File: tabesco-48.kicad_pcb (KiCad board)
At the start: 2 copper layers, 192.5 x 118.4 mm, 98 parts, among them SW1 SW_Push, U1 ProMicro

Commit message: created tabesco-31
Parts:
- removed D32, D33, D34, D35, D36, D37, D38, D39, D40, D41, D42, D43, D44, D45, D46, D47, D48: D_Small, Diode_SMD:D_SOD-123
- removed MX32, MX33, MX34, MX35, MX36, MX37, MX38, MX39, MX40, MX41, MX42, MX43, MX44, MX45, MX46, MX47, MX48: MX_SW_HS, marbastlib-mx:SW_MX_HS_CPG151101S11_1u
- added REF**: STAB_MX_6u, marbastlib-mx:STAB_MX_6u, F.Cu at (146.0, 89.3)
- U1: moved to B.Cu
- moved D1 182.9 mm to (60.3, 38.2), turned to 90 degrees
- moved MX1 182.5 mm to (60.3, 32.2)
- moved D11 178.2 mm to (65.0, 57.2), turned to 90 degrees
- moved MX11 177.8 mm to (65.0, 51.2)
- moved D10 164.7 mm to (231.7, 38.2), turned to 90 degrees
- moved MX10 164.3 mm to (231.7, 32.2)
- moved D30 164.1 mm to (79.3, 95.3), turned to 90 degrees
- moved MX30 163.6 mm to (79.3, 89.3)
- moved MX21 154.2 mm to (79.3, 70.3)
- moved D2 145.4 mm to (79.3, 38.2), turned to 90 degrees
- moved MX2 144.8 mm to (79.3, 32.2)
- moved D19 141.3 mm to (227.0, 57.2), turned to 90 degrees
- moved MX19 140.8 mm to (227.0, 51.2)
- moved D12 136.0 mm to (88.8, 57.2), turned to 90 degrees
- moved MX12 135.5 mm to (88.8, 51.2)
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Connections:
- D20 pad 1: /row1 -> /row2
- D29 pad 1: /row2 -> /row3
- MX20 pad 2: /col9 -> /col0
- MX21 pad 2: /col0 -> /col1
- MX22 pad 2: /col1 -> /col2
- MX23 pad 2: /col2 -> /col3
- MX24 pad 2: /col3 -> /col4
- MX25 pad 2: /col4 -> /col5
- MX26 pad 2: /col5 -> /col6
- MX27 pad 2: /col6 -> /col7
- MX28 pad 2: /col7 -> /col8
- MX29 pad 2: /col8 -> /col0
- MX30 pad 2: /col0 -> /col1
- MX31 pad 2: /col1 -> /col7
- U1 pad 5: /col_tmo -> unconnected-(U1-D1-Pad5)
- U1 pad 6: /row4 -> unconnected-(U1-D0-Pad6)
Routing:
- net /row4: track 292.9 -> 0.00 mm
- net /row3: track 276.5 -> 19.0 mm
- net /col8: track 228.5 -> 0.00 mm
- net /col7: track 211.5 -> 0.00 mm
- net /col9: track 209.3 -> 0.00 mm
- net /col6: track 195.2 -> 0.00 mm
- net /col5: track 176.7 -> 0.00 mm
- net /col4: track 157.6 -> 0.00 mm
- net /col3: track 142.6 -> 0.00 mm
- net /col2: track 136.9 -> 0.00 mm
- net /col0: track 111.3 -> 0.00 mm
- net /col1: track 96.1 -> 0.00 mm
- net /row2: track 243.4 -> 161.9 mm
- net /row1: track 242.0 -> 161.9 mm
- net GND: track 54.7 -> 0.00 mm
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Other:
- board size 192.5 x 118.4 mm -> 190.5 x 86.7 mm
- board text removed: "tabesco-48"

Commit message: work on 31
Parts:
- moved D28 123.8 mm to (222.2, 76.3)
- moved D27 114.3 mm to (193.6, 76.3)
- moved D26 47.6 mm to (174.6, 76.3)
- moved D23 38.1 mm to (117.4, 76.3)
- moved D21 38.1 mm to (79.3, 76.3)
- moved D22 38.1 mm to (98.4, 76.3)
- moved D24 38.1 mm to (136.5, 76.3)
- moved D25 38.1 mm to (155.5, 76.3)
- moved SW1 3.93 mm to (230.8, 95.7)
- moved U1 3.93 mm to (224.4, 93.2)
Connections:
- MX31 pad 2: /col7 -> /col5
- U1 pad 10: /row0 -> /col5
- U1 pad 11: /col0 -> /col6
- U1 pad 12: /col1 -> /col7
- U1 pad 17: /col2 -> /row0
- U1 pad 18: /col3 -> /row1
- U1 pad 19: /col4 -> /row2
- U1 pad 20: /col5 -> /row3
- U1 pad 21: /col6 -> unconnected-(U1-B1-Pad21)
- U1 pad 22: /col7 -> unconnected-(U1-B3-Pad22)
- U1 pad 5: unconnected-(U1-D1-Pad5) -> /col0
- U1 pad 6: unconnected-(U1-D0-Pad6) -> /col1
- U1 pad 7: /row3 -> /col2
- U1 pad 8: /row2 -> /col3
- U1 pad 9: /row1 -> /col4
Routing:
- net /col0: track 0.00 -> 308.7 mm
- net /col1: track 0.00 -> 296.8 mm
- net /col2: track 0.00 -> 260.0 mm
- net /row0: track 171.4 -> 416.5 mm
- net /col3: track 0.00 -> 242.2 mm
- net /col5: track 0.00 -> 231.9 mm
- net /row1: track 161.9 -> 388.4 mm
- net /col4: track 0.00 -> 224.5 mm
- net /row2: track 161.9 -> 361.3 mm
- net /col6: track 0.00 -> 188.7 mm
- net /col7: track 0.00 -> 171.2 mm
- net /col8: track 0.00 -> 167.7 mm
- net /row3: track 19.0 -> 166.4 mm
- net /col9: track 0.00 -> 96.6 mm
- net GND: track 0.00 -> 27.5 mm
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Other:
- board size 190.5 x 86.7 mm -> 196.2 x 86.7 mm

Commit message: tabesco31 pcb done(?)
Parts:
- removed SW1: SW_Push, Button_Switch_THT:SW_Tactile_Straight_KSA0Axx1LFTR
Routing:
- net RST: track 13.8 -> 0.00 mm
- net GND: track 27.5 -> 18.8 mm
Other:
- board text added: "swag bord"
- board text added: "tabesco-31"

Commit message: more work, transitioning to IC in seperate repo
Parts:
- added D32: D_Small, Diode_SMD:D_SOD-123, B.Cu at (166.9, 135.7)
- added D34: D_Small, Diode_SMD:D_SOD-123, B.Cu at (233.6, 135.7)
- added MX32: MX_SW_HS, marbastlib-mx:SW_MX_HS_CPG151101S11_1u, B.Cu at (166.9, 129.7)
- added MX32-2: MX_SW_HS, marbastlib-mx:SW_MX_HS_CPG151101S11_1u, B.Cu at (176.4, 129.7)
- added MX34: MX_SW_HS, marbastlib-mx:SW_MX_HS_CPG151101S11_1u, B.Cu at (233.6, 129.7)
- moved U1 109.3 mm to (123.9, 136.1)
- moved D31 61.1 mm to (100.2, 135.7)
- moved MX31 61.1 mm to (100.2, 129.7)
- moved REF** 45.5 mm to (166.9, 129.7)
- moved D1 40.4 mm to (62.1, 78.6)
- moved D10 40.4 mm to (233.6, 78.6)
- moved D2 40.4 mm to (81.2, 78.6)
- moved D3 40.4 mm to (100.2, 78.6)
- moved D4 40.4 mm to (119.3, 78.6)
- moved D5 40.4 mm to (138.3, 78.6)
- moved D6 40.4 mm to (157.4, 78.6)
- moved D7 40.4 mm to (176.4, 78.6)
- moved D8 40.4 mm to (195.5, 78.6)
- moved D9 40.4 mm to (214.5, 78.6)
- moved D11 40.4 mm to (66.9, 97.6)
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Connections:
- MX31 pad 2: /col5 -> /col2
- U1 pad 11: /col6 -> /col4
- U1 pad 12: /col7 -> /col3
- U1 pad 17: /row0 -> /row3
- U1 pad 18: /row1 -> /row2
- U1 pad 19: /row2 -> /row1
- U1 pad 20: /row3 -> /row0
- U1 pad 22: unconnected-(U1-B3-Pad22) -> /col2
- U1 pad 23: /col8 -> /col1
- U1 pad 24: /col9 -> /col0
- U1 pad 5: /col0 -> unconnected-(U1-D1-Pad5)
- U1 pad 6: /col1 -> /col9
- U1 pad 7: /col2 -> /col8
- U1 pad 8: /col3 -> /col7
- U1 pad 9: /col4 -> /col6
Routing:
- net /col0: track 308.7 -> 114.7 mm
- net /col1: track 296.8 -> 104.8 mm
- net /col2: track 260.0 -> 92.9 mm
- net /col3: track 242.2 -> 77.8 mm
- net /col4: track 224.5 -> 90.2 mm
- net /row0: track 416.5 -> 302.5 mm
- net /row1: track 388.4 -> 281.7 mm
- net /row2: track 361.3 -> 259.9 mm
- net /col9: track 96.6 -> 193.1 mm
- net /col5: track 231.9 -> 141.4 mm
- net /col8: track 167.7 -> 204.4 mm
- net Net-(D32-A): track 0.00 -> 25.5 mm
- net /col6: track 188.7 -> 164.9 mm
- net /row3: track 165.9 -> 180.0 mm
- net /col7: track 171.2 -> 161.2 mm
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
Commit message: brain mode
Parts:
- U1: moved to F.Cu
- moved U1 19.3 mm to (142.4, 130.6)
- moved MX7 0.45 mm to (176.7, 72.9)
- moved MX14 0.45 mm to (129.1, 91.9)
- moved MX26 0.45 mm to (176.7, 111.0)
- moved MX28 0.45 mm to (224.4, 111.0)
- moved MX32-2 0.45 mm to (176.7, 130.0)
- moved MX4 0.45 mm to (119.6, 72.9)
- moved MX1 0.45 mm to (62.4, 72.9)
- moved MX10 0.45 mm to (233.9, 72.9)
- moved MX11 0.45 mm to (67.2, 91.9)
- moved MX12 0.45 mm to (91.0, 91.9)
- moved MX2 0.45 mm to (81.5, 72.9)
- moved MX23 0.45 mm to (119.6, 111.0)
- moved MX3 0.45 mm to (100.5, 72.9)
- moved MX5 0.45 mm to (138.6, 72.9)
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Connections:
- U1 pad 10: /col5 -> /col8
- U1 pad 11: /col4 -> /col7
- U1 pad 12: /col3 -> /col6
- U1 pad 17: /row3 -> /col2
- U1 pad 18: /row2 -> /col1
- U1 pad 19: /row1 -> /col0
- U1 pad 20: /row0 -> unconnected-(U1-F7-Pad20)
- U1 pad 21: unconnected-(U1-B1-Pad21) -> /row0
- U1 pad 22: /col2 -> /row1
- U1 pad 23: /col1 -> /row2
- U1 pad 24: /col0 -> /row3
- U1 pad 6: /col9 -> /col3
- U1 pad 7: /col8 -> /col4
- U1 pad 8: /col7 -> /col5
- U1 pad 9: /col6 -> /col9
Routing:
- net /col6: track 164.9 -> 91.9 mm
- net /col7: track 161.2 -> 107.6 mm
- net /col0: track 114.7 -> 149.0 mm
- net /col8: track 204.4 -> 170.6 mm
- net /col5: track 141.4 -> 110.8 mm
- net /row2: track 259.9 -> 288.5 mm
- net /row1: track 281.7 -> 310.3 mm
- net /row0: track 302.5 -> 330.5 mm
- net /col1: track 104.8 -> 131.2 mm
- net /col4: track 90.2 -> 64.5 mm
- net /col2: track 92.9 -> 113.6 mm
- net /col9: track 193.1 -> 174.1 mm
- net /row3: track 180.0 -> 181.6 mm
- net /col3: track 77.8 -> 76.7 mm

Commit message: finished tabesco-34
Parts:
- removed MX32-2: MX_SW_HS, marbastlib-mx:SW_MX_HS_CPG151101S11_1u
- added D33: D_Small, Diode_SMD:D_SOD-123, B.Cu at (104.1, 106.0)
- added MX11-2: MX_SW_HS, marbastlib-mx:SW_MX_HS_CPG151101S11_1u, B.Cu at (63.8, 65.9)
- added MX19-2: MX_SW_HS, marbastlib-mx:SW_MX_HS_CPG151101S11_1u, B.Cu at (221.0, 65.9)
- added MX33: MX_SW_HS, marbastlib-mx:SW_MX_HS_CPG151101S11_1u, B.Cu at (111.4, 104.0)
- added MX34-2: MX_SW_HS, marbastlib-mx:SW_MX_HS_CPG151101S11_1u, B.Cu at (178.1, 104.0)
- U1: moved to B.Cu
- moved MX29 169.4 mm to (225.7, 84.9)
- moved D29 163.7 mm to (218.4, 86.9)
- moved D32 87.1 mm to (85.0, 106.0)
- moved MX32 79.2 mm to (92.4, 104.0)
- moved D34 78.2 mm to (161.2, 106.0)
- moved MX34 70.3 mm to (168.6, 104.0)
- moved U1 69.6 mm to (206.7, 104.0)
- moved D30 45.3 mm to (46.9, 106.0)
- moved D31 45.3 mm to (66.0, 106.0)
- moved D28 38.7 mm to (199.3, 86.9)
- moved MX30 37.7 mm to (54.3, 104.0)
- moved MX31 37.7 mm to (73.3, 104.0)
- moved D19 35.8 mm to (208.9, 67.9)
- moved D1 33.4 mm to (46.9, 48.8)
- moved D10 33.4 mm to (218.4, 48.8)
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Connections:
- D29 pad 1: /row3 -> /row2
- MX29 pad 2: /col0 -> /col9
- MX30 pad 2: /col1 -> /col0
- MX31 pad 2: /col2 -> /col1
- MX32 pad 2: /col5 -> /col2
- MX34 pad 2: /col8 -> /col6
- U1 pad 10: /col8 -> /row2
- U1 pad 11: /col7 -> /col8
- U1 pad 12: /col6 -> /row3
- U1 pad 17: /col2 -> /col0
- U1 pad 19: /col0 -> /col2
- U1 pad 20: unconnected-(U1-F7-Pad20) -> /col3
- U1 pad 21: /row0 -> /col7
- U1 pad 22: /row1 -> /col6
- U1 pad 23: /row2 -> /col5
- U1 pad 24: /row3 -> /col4
- U1 pad 6: /col3 -> unconnected-(U1-D0-Pad6)
- U1 pad 7: /col4 -> /row0
- U1 pad 8: /col5 -> /row1
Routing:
- net /col8: track 170.6 -> 71.0 mm
- net /col9: track 174.1 -> 76.4 mm
- net /col3: track 76.7 -> 164.4 mm
- net /row0: track 330.5 -> 250.1 mm
- net /row1: track 310.3 -> 230.5 mm
- net /col0: track 149.0 -> 226.5 mm
- net /col1: track 131.2 -> 208.6 mm
- net /col2: track 113.6 -> 186.4 mm
- net /col4: track 64.5 -> 125.2 mm
- net /col6: track 91.9 -> 120.9 mm
- net /col7: track 107.6 -> 81.9 mm
- net /row2: track 288.5 -> 263.3 mm
- net /row3: track 181.6 -> 206.7 mm, vias 0 -> 2
- net Net-(D32-A): track 25.6 -> 2.86 mm
- net Net-(D34-A): track 8.63 -> 23.3 mm
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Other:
- board size 196.2 x 86.7 mm -> 190.5 x 80 mm
- board text added: "tabesco-34"
- board text removed: "tabesco-31"

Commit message: swagbord case
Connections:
- MX11-2 pad 1: Net-(D11-A) -> /col0
- MX11-2 pad 2: /col0 -> Net-(D11-A)
- MX19-2 pad 1: Net-(D19-A) -> /col8
- MX19-2 pad 2: /col8 -> Net-(D19-A)
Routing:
- net /col8: track 71.0 -> 80.9 mm
- net Net-(D11-A): track 18.7 -> 11.5 mm
- net Net-(D19-A): track 18.7 -> 11.8 mm
- net /col0: track 226.5 -> 233.1 mm
- net /row1: track 230.5 -> 232.1 mm
- net Net-(D34-A): track 23.3 -> 24.4 mm
- net /row3: track 206.7 -> 207.6 mm
- net /row2: track 263.3 -> 263.9 mm
- net /col6: track 120.9 -> 121.5 mm

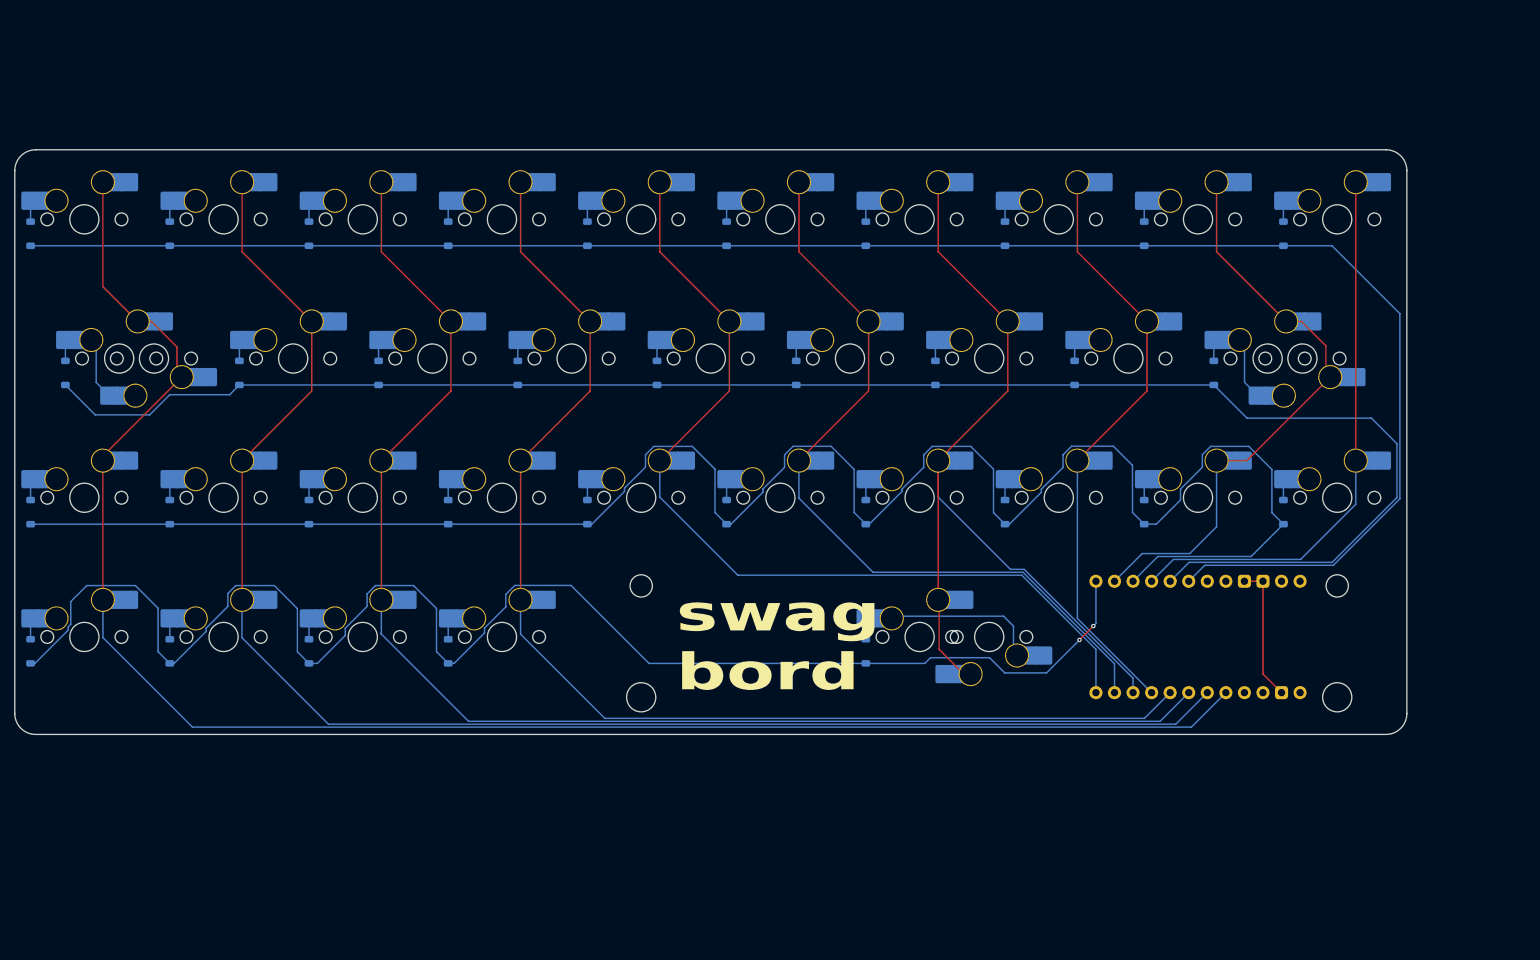
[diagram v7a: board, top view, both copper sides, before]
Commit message: fixed issue with usb C port placement
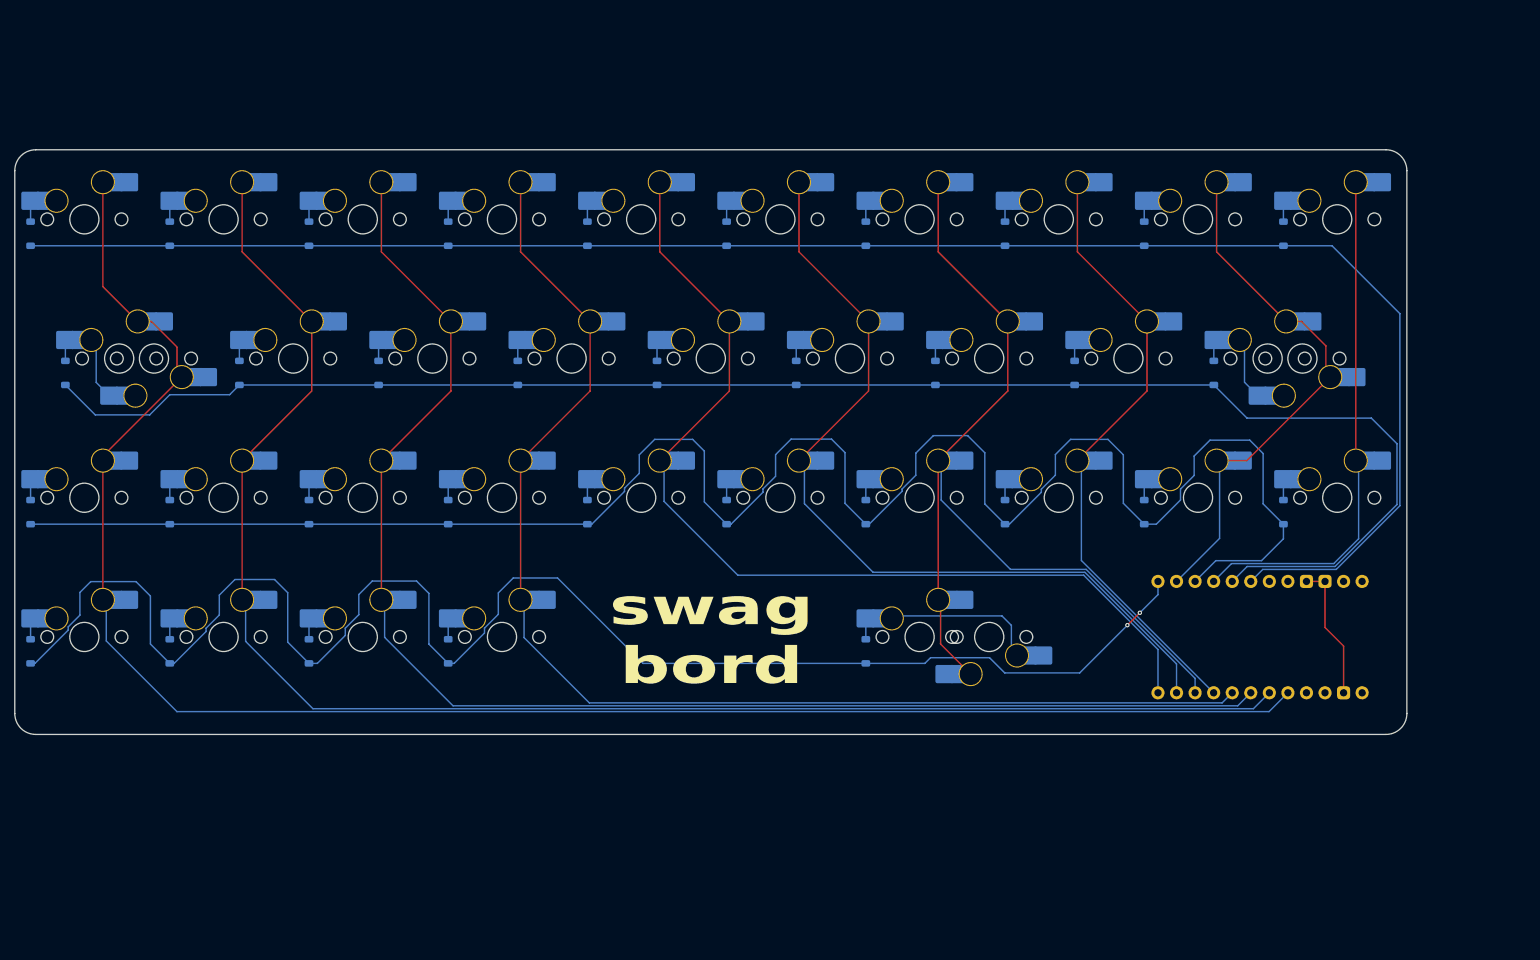
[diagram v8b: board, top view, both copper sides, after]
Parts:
- removed REF**: STAB_MX_6u, marbastlib-mx:STAB_MX_6u
- moved U1 8.49 mm to (215.2, 104.0)
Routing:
- net /row3: track 207.6 -> 219.6 mm
- net /col5: track 107.6 -> 116.1 mm
- net /col4: track 125.2 -> 133.7 mm
- net /col6: track 121.5 -> 129.4 mm
- net /row1: track 232.1 -> 224.2 mm
- net /row0: track 250.1 -> 242.2 mm
- net /col8: track 80.9 -> 74.1 mm
- net /col3: track 164.9 -> 171.6 mm
- net /col0: track 233.1 -> 239.8 mm
- net /col1: track 209.0 -> 215.7 mm
- net /col2: track 186.8 -> 193.5 mm
- net /col9: track 76.4 -> 71.2 mm
- net /col7: track 81.9 -> 85.5 mm
- net /row2: track 263.9 -> 266.6 mm
